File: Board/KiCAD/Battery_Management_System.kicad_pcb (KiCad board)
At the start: 4 copper layers, 47.7 x 62.6 mm, 117 parts, among them J1 Conn_01x06_Socket, J10 Conn_01x02, J11 Conn_01x02, J12 Conn_01x02, J13 Conn_01x02, J2 Conn_ARM_SWD_TagConnect_TC2030, J4 Conn_01x03, J5 Conn_01x03, J7 Conn_01x05, J8 Conn_01x02, J9 Conn_01x02, Q1 AON7408, Q10 AON7407, Q2 AON7408, Q23 2N7002, Q24 2N7002, Q25 2N7002, Q26 2N7002, Q3 AON7408, Q4 AON7408, Q5 BSS83P, Q6 BSS83P, Q7 BSS83P, Q8 BSS83P, SW2 SW_Push, U1 BQ25730RSNR, U3 LTC2943CDD#PBF, U5 LMR50410, U6 INA260, U7 INA260, U8 INA260, U9 STM32F103C8T6, Y1 Crystal_GND24_Small, Y4 CM8V-T1A-32.768KHZ-12.5PF-20P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

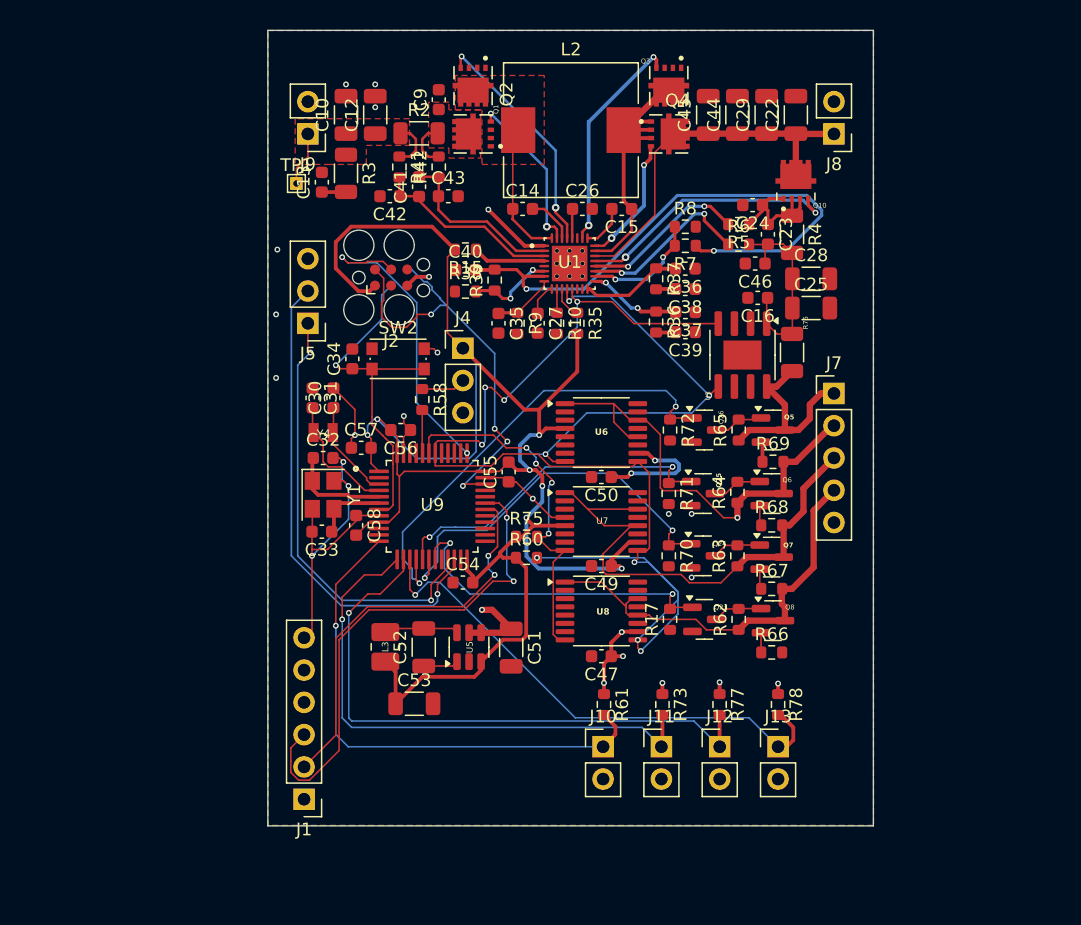
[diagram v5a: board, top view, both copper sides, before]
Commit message: Completed PCB Traceout
PCB Layout and traceout completed

@KeytarGoblin @Danish2PSU  @andrewgreenberg
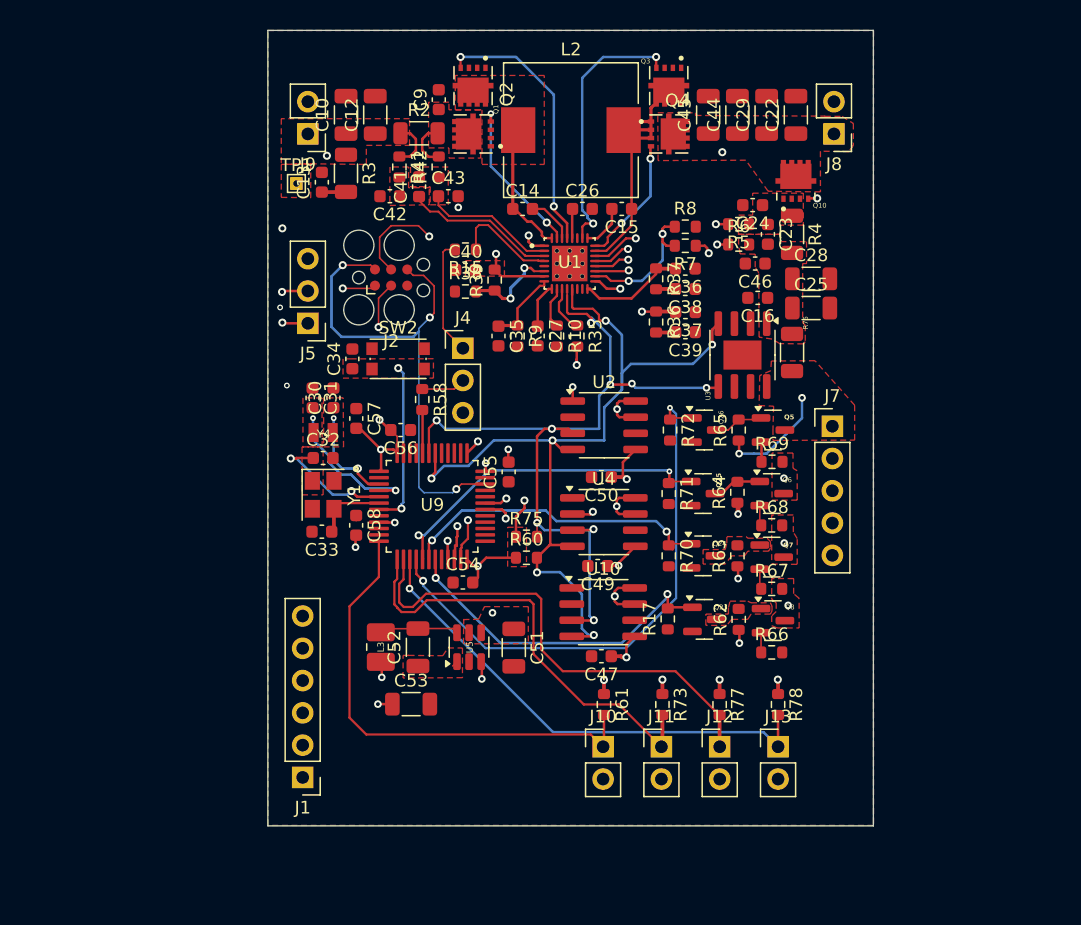
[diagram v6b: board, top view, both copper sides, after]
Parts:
- removed U6, U7, U8: INA260, Package_SO:TSSOP-16_4.4x5mm_P0.65mm
- added U10: INA219BxD, Package_SO:SOIC-8_3.9x4.9mm_P1.27mm, F.Cu at (229.5, 92.4)
- added U2: INA219BxD, Package_SO:SOIC-8_3.9x4.9mm_P1.27mm, F.Cu at (229.6, 77.7)
- added U4: INA219BxD, Package_SO:SOIC-8_3.9x4.9mm_P1.27mm, F.Cu at (229.6, 85.3)
- moved J7 2.58 mm to (247.6, 77.8)
- moved C57 2.34 mm to (210.1, 77.2), turned to -90 degrees
- moved J1 1.72 mm to (205.9, 105.4)
- moved C27 1.00 mm to (224.4, 70.7)
- moved C35 1.00 mm to (221.3, 70.7)
- moved R10 1.00 mm to (225.9, 70.7)
- moved R35 1.00 mm to (227.5, 70.7)
- moved R9 1.00 mm to (222.8, 70.7)
- moved C52 0.46 mm to (215.0, 95.2)
- moved L3 0.36 mm to (212.0, 95.2)
- moved C49 0.29 mm to (229.1, 88.8)
- moved C53 0.25 mm to (214.4, 99.7)
- moved C51 0.20 mm to (222.5, 95.2)
- moved R17 0.18 mm to (234.6, 93.0)
- moved R69 0.08 mm to (242.8, 80.6)
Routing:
- net 3.3V: track 171.3 -> 62.8 mm, vias 15 -> 22
- net GND: track 78.9 -> 24.3 mm, vias 17 -> 5
- net /Cell Interface/SCL: track 90.0 -> 68.0 mm, vias 8 -> 6
- net Net-(U3-SENSE+): track 16.1 -> 0.71 mm
- net /Charge Control/Vsys: track 29.1 -> 15.9 mm, vias 0 -> 2
- net /Cell Interface/Cell 2: track 41.0 -> 28.1 mm, vias 0 -> 3
- net /Charge Control/VBus: track 80.8 -> 67.9 mm, vias 2 -> 3
- net VDDA: track 45.1 -> 33.0 mm
- net Net-(U9-PC14-OSC32_IN): track 7.92 -> 19.8 mm, vias 0 -> 2
- net Net-(C23-Pad1): track 10.6 -> 0.04 mm
- net /Microcontroller/USART1_RX: track 40.5 -> 50.5 mm, vias 2 -> 1
- net /Microcontroller/I2C2_SDA_To_Host: track 38.5 -> 29.7 mm, vias 1 -> 2
- net /Microcontroller/Thermistor C2: track 43.7 -> 35.0 mm, vias 1 -> 0
- net /Microcontroller/I2C2_SCL_To_Host: track 34.5 -> 27.0 mm
- net /Cell Interface/BATT: track 16.2 -> 8.76 mm, vias 0 -> 2
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- added copper zone on F.Cu, net /Cell Interface/BATT
- added copper zone on F.Cu, net /Cell Interface/Cell 1
- added copper zone on F.Cu, net /Cell Interface/Cell 2
- added copper zone on F.Cu, net /Cell Interface/Cell 3
- added copper zone on F.Cu, net /Charge Control/Vsys
- added copper zone on F.Cu, net 3.3V
- added copper zone on F.Cu, net Net-(C23-Pad1)
- added copper zone on F.Cu, net Net-(J2-~{RESET})
- added copper zone on F.Cu, net Net-(Q23-D)
- added copper zone on F.Cu, net Net-(Q24-D)
- added copper zone on F.Cu, net Net-(U1-ACN)
- added copper zone on F.Cu, net Net-(U1-ACP)
- added copper zone on F.Cu, net Net-(U3-SENSE+)
- added copper zone on F.Cu, net Net-(U5-CB)
- added copper zone on F.Cu, net Net-(U9-PC14-OSC32_IN)
- added copper zone on F.Cu, net Net-(U9-PC15-OSC32_OUT)
- added copper zone on F.Cu, net Net-(U9-PD0_OSC_IN)
- added copper zone on F.Cu, net VDDA

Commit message: more updates
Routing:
- net GND: track 24.3 -> 4.28 mm
- net Net-(U9-PC14-OSC32_IN): track 19.8 -> 8.66 mm
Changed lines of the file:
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@@
 	)
 	(segment
-		(start 216.5 72)
-		(end 216.5 74.74)
-		(width 0.127)
-		(layer "In1.Cu")
-		(net 1)
-	)
-	(segment
-		(start 224 83.5)
-		(end 224 82.24)
-		(width 0.127)
-		(layer "In1.Cu")
-		(net 1)
-	)
-	(segment
-		(start 216.5 74.74)
-		(end 218.5 76.74)
-		(width 0.127)
-		(layer "In1.Cu")
-		(net 1)
-	)
-	(segment
-		(start 217.14 78.1)
-		(end 218.5 76.74)
-		(width 0.127)
-		(layer "In1.Cu")
-		(net 1)
-	)
-	(segment
-		(start 214.35 77)
-		(end 215.45 78.1)
-		(width 0.127)
-		(layer "In1.Cu")
-		(net 1)
-	)
-	(segment
-		(start 214.0712 77.0128)
-		(end 214.084 77)
-		(width 0.127)
-		(layer "In1.Cu")
-		(net 1)
-	)
-	(segment
-		(start 214.084 77)
-		(end 214.35 77)
-		(width 0.127)
-		(layer "In1.Cu")
-		(net 1)
-	)
-	(segment
-		(start 215.45 78.1)
-		(end 217.14 78.1)
-		(width 0.127)
-		(layer "In1.Cu")
-		(net 1)
-	)
-	(segment
-		(start 224 82.24)
-		(end 218.5 76.74)
-		(width 0.127)
-		(layer "In1.Cu")
-		(net 1)
-	)
-	(segment
 		(start 214.35 54.75)
 		(end 214.8 55.2)
@@
 	)
 	(segment
-		(start 210 84.625)
-		(end 206.625 88)
-		(width 0.127)
-		(layer "In1.Cu")
-		(net 13)
-	)
-	(segment
-		(start 209.7278 78.3844)
-		(end 210 78.6566)
-		(width 0.127)
-		(layer "In1.Cu")
-		(net 13)
-	)
-	(segment
-		(start 210 78.6566)
-		(end 210 84.625)
-		(width 0.127)
-		(layer "In1.Cu")
-		(net 13)
-	)
-	(segment
 		(start 211.895 82.85)
 		(end 213.2028 82.85)
@@
 	)
 	(segment
-		(start 246.38 59.8678)
-		(end 245.7072 59.8678)
-		(width 0.2)
-		(layer "F.Cu")
-		(net 34)
-	)
-	(segment
 		(start 231.065657 63.853243)
 		(end 230.1189 64.8)
@@
 	)
 	(segment
-		(start 230.1189 64.8)
-		(end 228.9 64.8)
-		(width 0.1778)
+		(start 246.7102 59.8678)
+		(end 245.7072 59.8678)
+		(width 0.2)
 		(layer "F.Cu")
 		(net 34)
@@
 	)
 	(segment
+		(start 230.1189 64.8)
+		(end 228.9 64.8)
+		(width 0.1778)
+		(layer "F.Cu")
+		(net 34)
+	)
+	(segment
 		(start 231.4956 63.853243)
 		(end 231.065657 63.853243)
@@
 	)
 	(via
-		(at 246.38 59.8678)
+		(at 246.7102 59.8678)
 		(size 0.635)
 		(drill 0.3302)
@@
 	)
 	(segment
-		(start 233.2482 62.749092)
-		(end 233.2482 58.4791)
+		(start 233.2482 58.501586)
+		(end 233.2482 62.749092)
 		(width 0.1778)
 		(layer "In2.Cu")
@@
 	)
 	(segment
-		(start 232.144049 63.853243)
-		(end 233.2482 62.749092)
+		(start 234.675986 57.0738)
+		(end 233.2482 58.501586)
 		(width 0.1778)
 		(layer "In2.Cu")
@@
 	)
 	(segment
-		(start 233.2482 58.4791)
-		(end 234.6535 57.0738)
+		(start 246.38 59.5376)
+		(end 246.38 57.7596)
 		(width 0.1778)
 		(layer "In2.Cu")
@@
 	(segment
 		(start 246.38 57.7596)
-		(end 246.38 59.8678)
+		(end 245.6942 57.0738)
 		(width 0.1778)
 		(layer "In2.Cu")
@@
 	)
 	(segment
-		(start 245.6942 57.0738)
-		(end 246.38 57.7596)
+		(start 233.2482 62.749092)
+		(end 232.144049 63.853243)
 		(width 0.1778)
 		(layer "In2.Cu")
@@
 	)
 	(segment
-		(start 234.6535 57.0738)
-		(end 245.6942 57.0738)
+		(start 232.144049 63.853243)
+		(end 231.4956 63.853243)
 		(width 0.1778)
 		(layer "In2.Cu")
@@
 	)
 	(segment
-		(start 231.4956 63.853243)
-		(end 232.144049 63.853243)
+		(start 245.6942 57.0738)
+		(end 234.675986 57.0738)
+		(width 0.1778)
+		(layer "In2.Cu")
+		(net 34)
+	)
+	(segment
+		(start 246.7102 59.8678)
+		(end 246.38 59.5376)
 		(width 0.1778)
 		(layer "In2.Cu")
@@
 	(via
 		(at 234.7468 81.3562)
-		(size 0.4572)
-		(drill 0.2032)
+		(size 0.635)
+		(drill 0.3302)
 		(layers "F.Cu" "B.Cu")
 		(free yes)
@@
 	(via
 		(at 234.7976 76.3524)
-		(size 0.4572)
-		(drill 0.2032)
+		(size 0.635)
+		(drill 0.3302)
 		(layers "F.Cu" "B.Cu")
 		(free yes)
@@
 	(via
 		(at 244.094 91.8972)
-		(size 0.6)
-		(drill 0.3)
+		(size 0.635)
+		(drill 0.3302)
 		(layers "F.Cu" "B.Cu")
 		(free yes)
@@
 	(via
 		(at 240.157 89.789)
-		(size 0.6)
-		(drill 0.3)
+		(size 0.635)
+		(drill 0.3302)
 		(layers "F.Cu" "B.Cu")
 		(net 44)
@@
 	(via
 		(at 243.7892 86.995)
-		(size 0.6)
-		(drill 0.3)
+		(size 0.635)
+		(drill 0.3302)
 		(layers "F.Cu" "B.Cu")
 		(free yes)
@@
 	(via
 		(at 243.7638 81.8896)
-		(size 0.6)
-		(drill 0.3)
+		(size 0.635)
+		(drill 0.3302)
 		(layers "F.Cu" "B.Cu")
 		(free yes)
@@
 	(via
 		(at 240.157 84.709)
-		(size 0.6)
-		(drill 0.3)
+		(size 0.635)
+		(drill 0.3302)
 		(layers "F.Cu" "B.Cu")
 		(net 45)
@@
 	(via
 		(at 245.1862 75.565)
-		(size 0.6)
-		(drill 0.3)
+		(size 0.635)
+		(drill 0.3302)
 		(layers "F.Cu" "B.Cu")
 		(free yes)

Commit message: current form
current form of pcb @andrewgreenberg
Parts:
- removed U10, U2, U4: INA219BxD, Package_SO:SOIC-8_3.9x4.9mm_P1.27mm
- added U6: INA219AxDCN, Package_TO_SOT_SMD:SOT-23-8, F.Cu at (263.4, 71.3)
- added U7: INA219AxDCN, Package_TO_SOT_SMD:SOT-23-8, F.Cu at (263.4, 75.9)
- added U8: INA219AxDCN, Package_TO_SOT_SMD:SOT-23-8, F.Cu at (263.4, 80.5)
